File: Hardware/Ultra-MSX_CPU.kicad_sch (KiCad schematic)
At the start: 23 parts, among them J15 Battery_2x_SR66_holder, J2 F_PANEL, U1 MPU_Z380, U5 BQ4802YPW, Y2 32768 Hz

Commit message: Routed the VDP-board further, as well as making it a 4-layer board - also added an exception in the gitignore, for big images.
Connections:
- net ENG_~{INT}/INIT renamed ENG_~{INT}
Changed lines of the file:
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@@
     (stroke (width 0) (type default) (color 0 0 0 0))
   )
-  (wire (pts (xy 22.86 62.23) (xy 36.83 62.23))
+  (wire (pts (xy 26.67 62.23) (xy 36.83 62.23))
     (stroke (width 0) (type default) (color 0 0 0 0))
   )
@@
     (effects (font (size 1.524 1.524)) (justify right bottom))
   )
-  (label "ENG_~{INT}{slash}INIT" (at 22.86 62.23 0)
+  (label "ENG_~{INT}" (at 26.67 62.23 0)
     (effects (font (size 1.54 1.54)) (justify left bottom))
   )
@@
     (effects (font (size 1.524 1.524)) (justify left bottom))
   )
-  (label "ENG_~{INT}{slash}INIT" (at 346.71 21.59 0)
+  (label "ENG_~{INT}" (at 346.71 21.59 0)
     (effects (font (size 1.54 1.54)) (justify left bottom))
   )
@@
     (effects (font (size 1.27 1.27)) (justify left))
   )
-  (hierarchical_label "ENG_~{INT}{slash}INIT" (shape input) (at 361.95 21.59 0)
+  (hierarchical_label "ENG_~{INT}" (shape input) (at 361.95 21.59 0)
     (effects (font (size 1.54 1.54)) (justify left))
   )

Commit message: Finished the VDP-board, finished up the mixer-section, removed the buffer-pins from the FPGA, and instead added external buffers for the slots, designed a marquee-block with the Ultra-MSX logo, designed the logotype, andmultiple other changes.
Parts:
- R62, R63, R64, R65, R66, R67, R68, R69: footprint Resistor_SMD:R_0603_1608Metric_Pad0.98x0.95mm_HandSolder -> LRJ:R_0603_1608Metric_roundcourt
- renumbered J2 to J11

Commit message: Added SD-card slot, made basic 3d-model for sd-card slot, connected it up in the schematic, and numerous other tweaks.
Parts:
- J11: value F_PANEL -> Conn_02x05_Odd_Even
- R26: value 100k -> R
- Y2: value 32768 Hz -> Crystal_AB38T-32.768KHZ
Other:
- note added: "MSX-engine chips: ------------ PPI ---- v-7400 (four 2-input NAND) -7430 (x2) (8-input NAND) -7432 (x3) (four 2-input OR) -74273 (x2) (eight D-type flip-flop with reset; positive-edge trigger) -74540 (Octal buffer/line driver; inverting) -74541 (x3) (8-bit Buffer/Line Driver) -74153 (x2) (two 4-input multiplexer) -8255 Logic: 7x2 NAND + 4 NAND (18 NAND) 4x3 OR (36 NAND) 8x2 Flip-flop (96 NAND) 1x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"
- note removed: "MSX-engine chips: ------------ PPI ---- -7400 (four 2-input NAND) -7430 (x2) (8-input NAND) -7432 (x3) (four 2-input OR) -74273 (x2) (eight D-type flip-flop with reset; positive-edge trigger) -74540 (Octal buffer/line driver; inverting) -74541 (x3) (8-bit Buffer/Line Driver) -74153 (x2) (two 4-input multiplexer) -8255 Logic: 7x2 NAND + 4 NAND (18 NAND) 4x3 OR (36 NAND) 8x2 Flip-flop (96 NAND) 1x8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"
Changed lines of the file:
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@@
     (effects (font (size 1.524 1.524)) (justify left bottom))
   )
-  (text "MSX-engine chips:\n------------\nPPI\n----\n-7400 (four 2-input NAND)\n-7430 (x2) (8-input NAND)\n-7432 (x3) (four 2-input OR)\n-74273 (x2) (eight D-type flip-flop with reset; positive-edge trigger)\n-74540 (Octal buffer/line driver; inverting)\n-74541 (x3) (8-bit Buffer/Line Driver)\n-74153 (x2) (two 4-input multiplexer)\n-8255\n\nLogic:\n7x2 NAND + 4 NAND (18 NAND)\n4x3 OR (36 NAND) \n8x2 Flip-flop (96 NAND)\n1x8-bit buffer +8 NOT (47 NAND)\n3x8-bit buffer (117 NAND)\n2x Mul (168 NAND)\n2300 NAND\n\nTotal:\n2782 GATES\n--\n\nMemory\n-------\n-74138 (Decoder/demultiplexer, 3to8)\n-74245 (x2) (octal Bus Transceiver)\n\nLogic:\n1x Dmul (84 NAND)\n2x Tran (78 NAND)\n\nTotal:\n162 GATES\n--\n\nVDP-support:\n---\n7404 (hex inverter)\n\nLogic:\n6 NOT (6 NAND)\n\n\n--\n\nPSG\n---\n-7407 (hex-buffer)\n7474 (x3) (two D-type flip-flop with set & reset)\n7402 (four 2-input NOR)\n74157 x2 (four 2-input Multiplexer)\n\nLogic:\n1 buf (36 NAND)\n3x2 Flip-flop (36 NAND)\n4x NOR (16 NAND)\n--\nTotal:\n88 GATES\n\nCPU\n---\nRP5C01 (x1) (real-time clock)\nATF16V8B (x3) (SPLD, 8 macrocell)\n74175 (four D-type flip-flop with reset; positive-edge trigger)\n\nLogic:\nxx\n3x8 MAC (1800 NAND)\n4x Flip-Flop (24 NAND)\n\n----\nTOTAL GATES:\n4862 GATES\n@6 gates / LUT\n811 LUTs\n\nW. 25% overprovisioning\n6078 Gates\n1014 LUTs\n\nSuggested chips:\n5V:\n\nAT40K10-2DQU\nAT40K20-2EQJ (1024 LUTs)\n\n3.3V:\nXC95288XL-10BGG256C\nXC95288XL-7FGG256I\n\n--\n\nTOTAL IO:\n183 I/O\n\n\n----\nQUESTION:\n--\nHow many of the chips are already replaced via the Z280?\n\n\nAnalogue chips:\n-----------------\n74125 (four level-shifters - 3to5V)\nADM691A (Voltage monitor)\nCXA1645 (RGB encoder)\n"
+  (text "MSX-engine chips:\n------------\nPPI\n----\nv-7400 (four 2-input NAND)\n-7430 (x2) (8-input NAND)\n-7432 (x3) (four 2-input OR)\n-74273 (x2) (eight D-type flip-flop with reset; positive-edge trigger)\n-74540 (Octal buffer/line driver; inverting)\n-74541 (x3) (8-bit Buffer/Line Driver)\n-74153 (x2) (two 4-input multiplexer)\n-8255\n\nLogic:\n7x2 NAND + 4 NAND (18 NAND)\n4x3 OR (36 NAND) \n8x2 Flip-flop (96 NAND)\n1x8-bit buffer +8 NOT (47 NAND)\n3x8-bit buffer (117 NAND)\n2x Mul (168 NAND)\n2300 NAND\n\nTotal:\n2782 GATES\n--\n\nMemory\n-------\n-74138 (Decoder/demultiplexer, 3to8)\n-74245 (x2) (octal Bus Transceiver)\n\nLogic:\n1x Dmul (84 NAND)\n2x Tran (78 NAND)\n\nTotal:\n162 GATES\n--\n\nVDP-support:\n---\n7404 (hex inverter)\n\nLogic:\n6 NOT (6 NAND)\n\n\n--\n\nPSG\n---\n-7407 (hex-buffer)\n7474 (x3) (two D-type flip-flop with set & reset)\n7402 (four 2-input NOR)\n74157 x2 (four 2-input Multiplexer)\n\nLogic:\n1 buf (36 NAND)\n3x2 Flip-flop (36 NAND)\n4x NOR (16 NAND)\n--\nTotal:\n88 GATES\n\nCPU\n---\nRP5C01 (x1) (real-time clock)\nATF16V8B (x3) (SPLD, 8 macrocell)\n74175 (four D-type flip-flop with reset; positive-edge trigger)\n\nLogic:\nxx\n3x8 MAC (1800 NAND)\n4x Flip-Flop (24 NAND)\n\n----\nTOTAL GATES:\n4862 GATES\n@6 gates / LUT\n811 LUTs\n\nW. 25% overprovisioning\n6078 Gates\n1014 LUTs\n\nSuggested chips:\n5V:\n\nAT40K10-2DQU\nAT40K20-2EQJ (1024 LUTs)\n\n3.3V:\nXC95288XL-10BGG256C\nXC95288XL-7FGG256I\n\n--\n\nTOTAL IO:\n183 I/O\n\n\n----\nQUESTION:\n--\nHow many of the chips are already replaced via the Z280?\n\n\nAnalogue chips:\n-----------------\n74125 (four level-shifters - 3to5V)\nADM691A (Voltage monitor)\nCXA1645 (RGB encoder)\n"
     (at 425.45 282.575 0)
     (effects (font (size 1.524 1.524)) (justify left bottom))
@@
     (in_bom yes) (on_board yes)
     (property "Reference" "J11" (id 0) (at 140.97 118.11 0))
-    (property "Value" "F_PANEL" (id 1) (at 140.97 133.35 0))
+    (property "Value" "Conn_02x05_Odd_Even" (id 1) (at 140.97 133.35 0))
     (property "Footprint" "Connector_PinHeader_2.54mm:PinHeader_2x05_P2.54mm_Vertical_SMD" (id 2) (at 139.7 125.73 0)
       (effects (font (size 1.27 1.27)) hide)
@@
     (in_bom yes) (on_board yes)
     (property "Reference" "R26" (id 0) (at 46.228 180.34 90))
-    (property "Value" "100k" (id 1) (at 48.26 180.34 90))
+    (property "Value" "R" (id 1) (at 48.26 180.34 90))
     (property "Footprint" "Resistor_SMD:R_0805_2012Metric" (id 2) (at 50.038 180.34 90)
       (effects (font (size 1.27 1.27)) hide)
@@
       (effects (font (size 1.27 1.27) bold))
     )
-    (property "Value" "32768 Hz" (id 1) (at 53.34 176.53 90))
+    (property "Value" "Crystal_AB38T-32.768KHZ" (id 1) (at 53.34 176.53 90))
     (property "Footprint" "Ultra-MSX:Crystal_32K_Horiz" (id 2) (at 60.96 171.45 0)
       (effects (font (size 1.27 1.27)) hide)

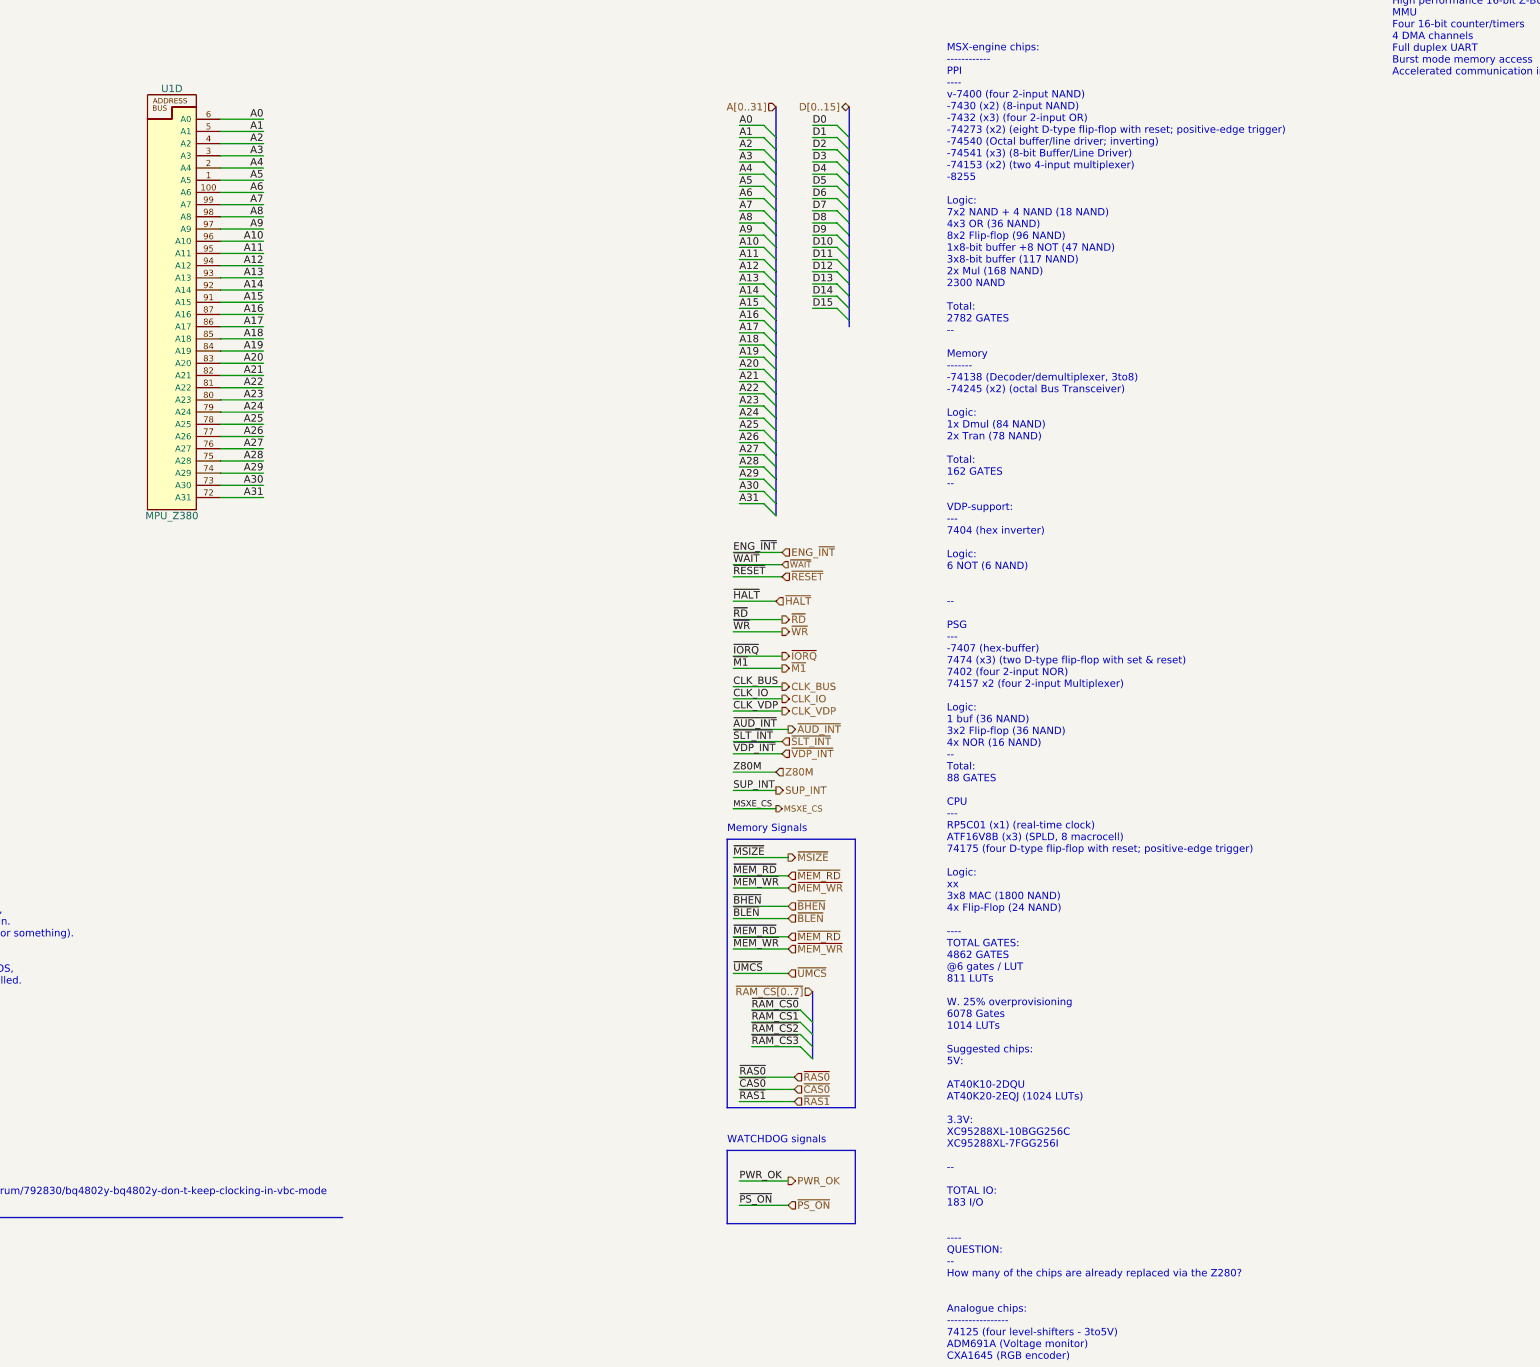
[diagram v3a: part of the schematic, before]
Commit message: Redesigned VDP-board to include a socket, increased it to 4 layers. Various clean-ups here and there. Improved the printer-port and joystick-port 3D-models. Improved the cooling-fin 3D-model, and added attachment-spring in 3D-model.
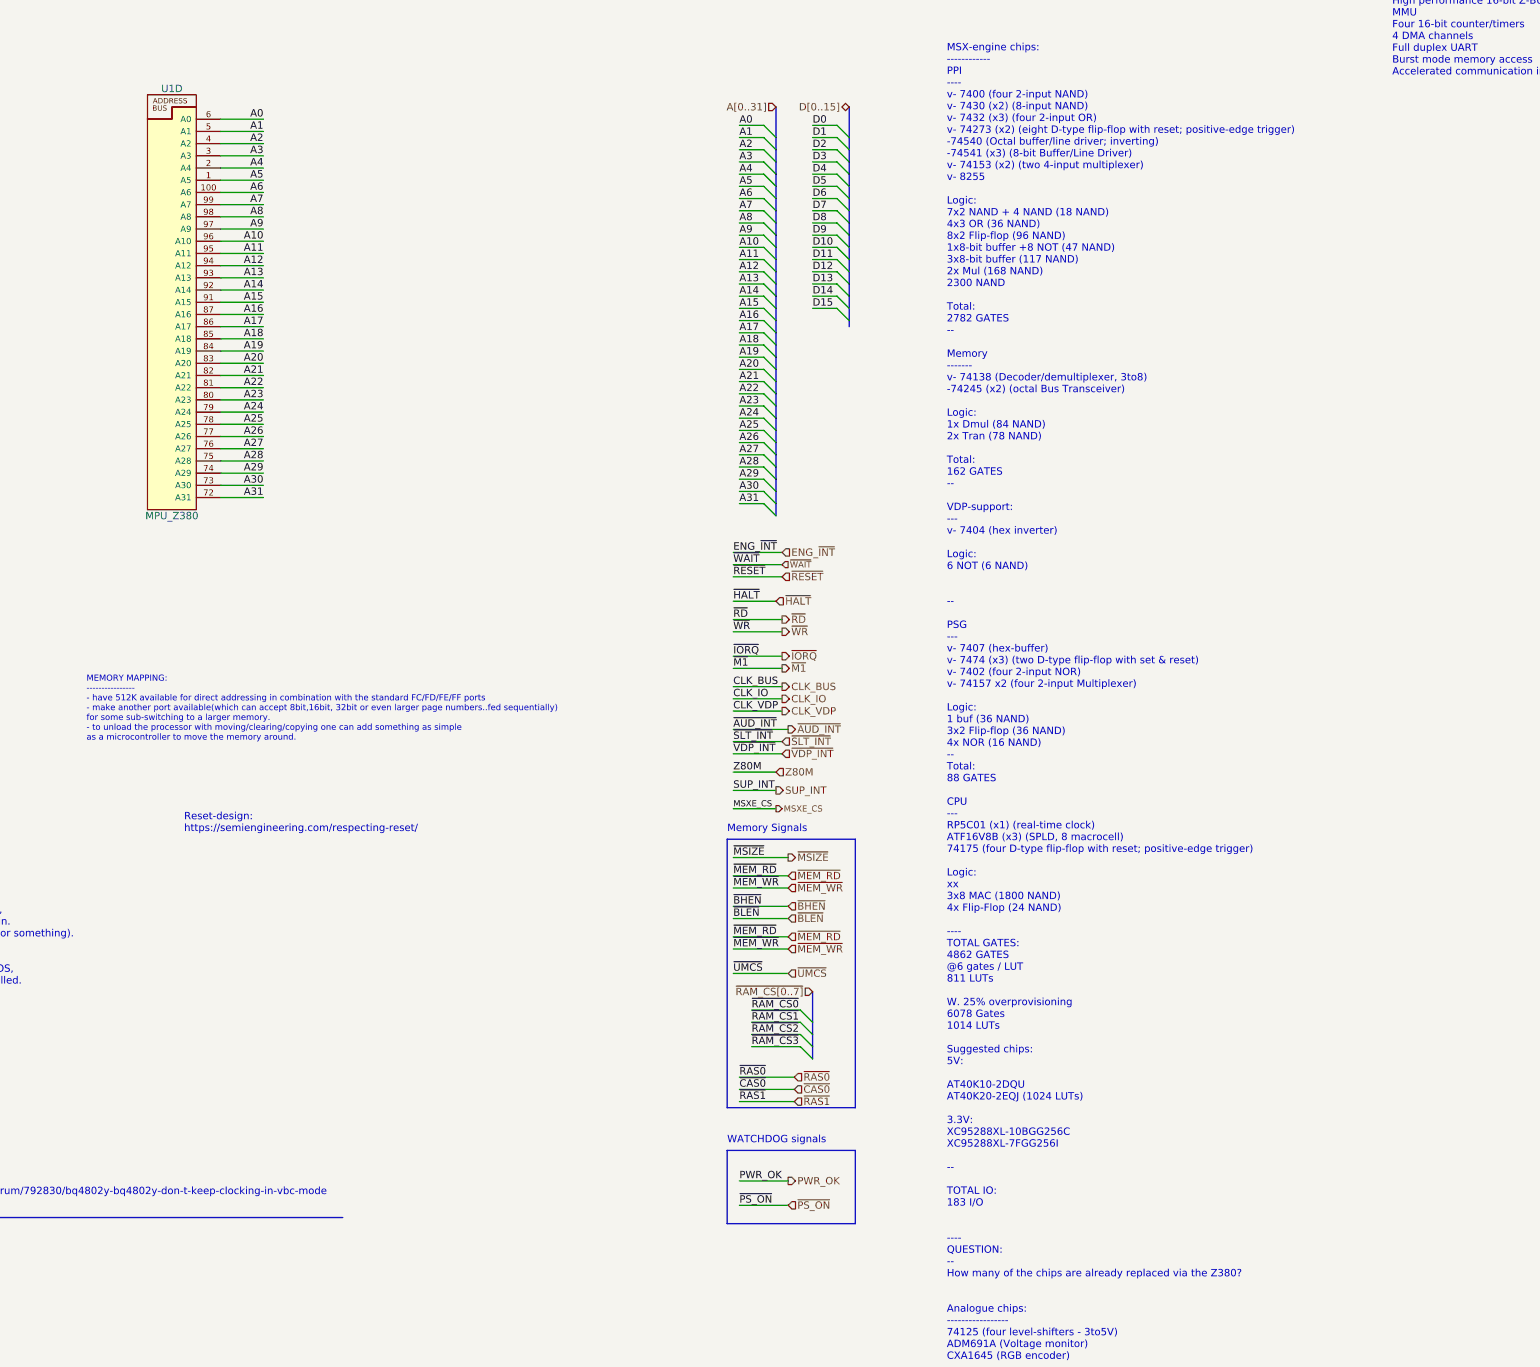
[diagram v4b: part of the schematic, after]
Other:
- note added: "MEMORY MAPPING: ---------------- - have 512K available for direct addressing in combination with the standard FC/FD/FE/FF ports - make another port available(which can accept 8bit,16bit, 32bit or even larger page numbers..fed sequentially) for some sub-switching to a larger memory. - to unload the processor with moving/clearing/copying one can add something as simple as a microcontroller to move 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"
- note added: "MSX-engine chips: ------------ PPI ---- v- 7400 (four 2-input NAND) v- 7430 (x2) (8-input NAND) v- 7432 (x3) (four 2-input OR) v- 74273 (x2) (eight D-type flip-flop with reset; positive-edge trigger) -74540 (Octal buffer/line driver; inverting) -74541 (x3) (8-bit Buffer/Line Driver) v- 74153 (x2) (two 4-input multiplexer) v- 8255 Logic: 7x2 NAND + 4 NAND (18 NAND) 4x3 OR (36 NAND) 8x2 Flip-flop (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"
- note added: "Reset-design: https://semiengineering.com/respecting-reset/"
- note removed: "MSX-engine chips: ------------ PPI ---- v-7400 (four 2-input NAND) -7430 (x2) (8-input NAND) -7432 (x3) (four 2-input OR) -74273 (x2) (eight D-type flip-flop with reset; positive-edge trigger) -74540 (Octal buffer/line driver; inverting) -74541 (x3) (8-bit Buffer/Line Driver) -74153 (x2) (two 4-input multiplexer) -8255 Logic: 7x2 NAND + 4 NAND (18 NAND) 4x3 OR (36 NAND) 8x2 Flip-flop (96 NAND) 1x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"
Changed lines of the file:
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@@
+    (effects (font (size 1.524 1.524)) (justify left bottom))
+  )
+  (text "Reset-design:\nhttps://semiengineering.com/respecting-reset/"
+    (at 266.7 172.72 0)
     (effects (font (size 1.524 1.524)) (justify left bottom))
   )
@@
     (effects (font (size 1.524 1.524)) (justify left bottom))
   )
-  (text "MSX-engine chips:\n------------\nPPI\n----\nv-7400 (four 2-input NAND)\n-7430 (x2) (8-input NAND)\n-7432 (x3) (four 2-input OR)\n-74273 (x2) (eight D-type flip-flop with reset; positive-edge trigger)\n-74540 (Octal buffer/line driver; inverting)\n-74541 (x3) (8-bit Buffer/Line Driver)\n-74153 (x2) (two 4-input multiplexer)\n-8255\n\nLogic:\n7x2 NAND + 4 NAND (18 NAND)\n4x3 OR (36 NAND) \n8x2 Flip-flop (96 NAND)\n1x8-bit buffer +8 NOT (47 NAND)\n3x8-bit buffer (117 NAND)\n2x Mul (168 NAND)\n2300 NAND\n\nTotal:\n2782 GATES\n--\n\nMemory\n-------\n-74138 (Decoder/demultiplexer, 3to8)\n-74245 (x2) (octal Bus Transceiver)\n\nLogic:\n1x Dmul (84 NAND)\n2x Tran (78 NAND)\n\nTotal:\n162 GATES\n--\n\nVDP-support:\n---\n7404 (hex inverter)\n\nLogic:\n6 NOT (6 NAND)\n\n\n--\n\nPSG\n---\n-7407 (hex-buffer)\n7474 (x3) (two D-type flip-flop with set & reset)\n7402 (four 2-input NOR)\n74157 x2 (four 2-input Multiplexer)\n\nLogic:\n1 buf (36 NAND)\n3x2 Flip-flop (36 NAND)\n4x NOR (16 NAND)\n--\nTotal:\n88 GATES\n\nCPU\n---\nRP5C01 (x1) (real-time clock)\nATF16V8B (x3) (SPLD, 8 macrocell)\n74175 (four D-type flip-flop with reset; positive-edge trigger)\n\nLogic:\nxx\n3x8 MAC (1800 NAND)\n4x Flip-Flop (24 NAND)\n\n----\nTOTAL GATES:\n4862 GATES\n@6 gates / LUT\n811 LUTs\n\nW. 25% overprovisioning\n6078 Gates\n1014 LUTs\n\nSuggested chips:\n5V:\n\nAT40K10-2DQU\nAT40K20-2EQJ (1024 LUTs)\n\n3.3V:\nXC95288XL-10BGG256C\nXC95288XL-7FGG256I\n\n--\n\nTOTAL IO:\n183 I/O\n\n\n----\nQUESTION:\n--\nHow many of the chips are already replaced via the Z280?\n\n\nAnalogue chips:\n-----------------\n74125 (four level-shifters - 3to5V)\nADM691A (Voltage monitor)\nCXA1645 (RGB encoder)\n"
+  (text "MEMORY MAPPING:\n----------------\n- have 512K available for direct addressing in combination with the standard FC/FD/FE/FF ports\n- make another port available(which can accept 8bit,16bit, 32bit or even larger page numbers..fed sequentially) \nfor some sub-switching to a larger memory.\n- to unload the processor with moving/clearing/copying one can add something as simple \nas a microcontroller to move the memory around."
+    (at 246.38 153.67 0)
+    (effects (font (size 1.27 1.27)) (justify left bottom))
+  )
+  (text "MSX-engine chips:\n------------\nPPI\n----\nv- 7400 (four 2-input NAND)\nv- 7430 (x2) (8-input NAND)\nv- 7432 (x3) (four 2-input OR)\nv- 74273 (x2) (eight D-type flip-flop with reset; positive-edge trigger)\n-74540 (Octal buffer/line driver; inverting)\n-74541 (x3) (8-bit Buffer/Line Driver)\nv- 74153 (x2) (two 4-input multiplexer)\nv- 8255\n\nLogic:\n7x2 NAND + 4 NAND (18 NAND)\n4x3 OR (36 NAND) \n8x2 Flip-flop (96 NAND)\n1x8-bit buffer +8 NOT (47 NAND)\n3x8-bit buffer (117 NAND)\n2x Mul (168 NAND)\n2300 NAND\n\nTotal:\n2782 GATES\n--\n\nMemory\n-------\nv- 74138 (Decoder/demultiplexer, 3to8)\n-74245 (x2) (octal Bus Transceiver)\n\nLogic:\n1x Dmul (84 NAND)\n2x Tran (78 NAND)\n\nTotal:\n162 GATES\n--\n\nVDP-support:\n---\nv- 7404 (hex inverter)\n\nLogic:\n6 NOT (6 NAND)\n\n\n--\n\nPSG\n---\nv- 7407 (hex-buffer)\nv- 7474 (x3) (two D-type flip-flop with set & reset)\nv- 7402 (four 2-input NOR)\nv- 74157 x2 (four 2-input Multiplexer)\n\nLogic:\n1 buf (36 NAND)\n3x2 Flip-flop (36 NAND)\n4x NOR (16 NAND)\n--\nTotal:\n88 GATES\n\nCPU\n---\nRP5C01 (x1) (real-time clock)\nATF16V8B (x3) (SPLD, 8 macrocell)\n74175 (four D-type flip-flop with reset; positive-edge trigger)\n\nLogic:\nxx\n3x8 MAC (1800 NAND)\n4x Flip-Flop (24 NAND)\n\n----\nTOTAL GATES:\n4862 GATES\n@6 gates / LUT\n811 LUTs\n\nW. 25% overprovisioning\n6078 Gates\n1014 LUTs\n\nSuggested chips:\n5V:\n\nAT40K10-2DQU\nAT40K20-2EQJ (1024 LUTs)\n\n3.3V:\nXC95288XL-10BGG256C\nXC95288XL-7FGG256I\n\n--\n\nTOTAL IO:\n183 I/O\n\n\n----\nQUESTION:\n--\nHow many of the chips are already replaced via the Z380?\n\n\nAnalogue chips:\n-----------------\n74125 (four level-shifters - 3to5V)\nADM691A (Voltage monitor)\nCXA1645 (RGB encoder)\n"
     (at 425.45 282.575 0)
     (effects (font (size 1.524 1.524)) (justify left bottom))

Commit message: Generated first PDF-files
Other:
- moved on the sheet: U1D
